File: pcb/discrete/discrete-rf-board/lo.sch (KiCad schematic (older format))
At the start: 52 parts, among them J14 UFL, J15 UFL, Q11 BFU520R, U5 ADF4360-7BCPZRL7, U6 HHM17147A1, X1 ECS-5032MV-100-BN-TR

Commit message: Autofill
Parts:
- C100, C101, C106, C107, C211, C94: footprint (none) -> Capacitor_SMD:C_0402_1005Metric; Mouser (none) -> 791-RF15N101J250CT
- R72, R74: footprint (none) -> Capacitor_SMD:C_0402_1005Metric; Mouser (none) -> 71-CRCW04020000Z0EDC
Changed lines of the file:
@@
 F 0 "R72" H 7680 4220 50  0000 L CNN
 F 1 "0R" H 7680 4160 50  0000 L CNN
-F 2 "" H 7650 4200 50  0001 C CNN
+F 2 "Capacitor_SMD:C_0402_1005Metric" H 7650 4200 50  0001 C CNN
 F 3 "~" H 7650 4200 50  0001 C CNN
+F 4 "71-CRCW04020000Z0EDC" H 7650 4200 50  0001 C CNN "Mouser"
 	1    7650 4200
 	0    -1   1    0
@@
 F 0 "R74" H 8180 4220 50  0000 L CNN
 F 1 "0R" H 8180 4160 50  0000 L CNN
-F 2 "" H 8150 4200 50  0001 C CNN
+F 2 "Capacitor_SMD:C_0402_1005Metric" H 8150 4200 50  0001 C CNN
 F 3 "~" H 8150 4200 50  0001 C CNN
+F 4 "71-CRCW04020000Z0EDC" H 8150 4200 50  0001 C CNN "Mouser"
 	1    8150 4200
 	0    -1   1    0
@@
 F 0 "C106" H 9610 3970 50  0000 L CNN
 F 1 "100 pF" H 9610 3820 50  0000 L CNN
-F 2 "" H 9600 3900 50  0001 C CNN
+F 2 "Capacitor_SMD:C_0402_1005Metric" H 9600 3900 50  0001 C CNN
 F 3 "~" H 9600 3900 50  0001 C CNN
+F 4 "791-RF15N101J250CT " H 9600 3900 50  0001 C CNN "Mouser"
 	1    9600 3900
 	0    -1   -1   0
@@
 F 0 "C107" H 10160 3070 50  0000 L CNN
 F 1 "100 pF" H 10160 2920 50  0000 L CNN
-F 2 "" H 10150 3000 50  0001 C CNN
+F 2 "Capacitor_SMD:C_0402_1005Metric" H 10150 3000 50  0001 C CNN
 F 3 "~" H 10150 3000 50  0001 C CNN
+F 4 "791-RF15N101J250CT " H 10150 3000 50  0001 C CNN "Mouser"
 	1    10150 3000
 	1    0    0    -1
@@
 F 0 "C94" H 5410 2320 50  0000 L CNN
 F 1 "100 pF" H 5410 2170 50  0000 L CNN
-F 2 "" H 5400 2250 50  0001 C CNN
+F 2 "Capacitor_SMD:C_0402_1005Metric" H 5400 2250 50  0001 C CNN
 F 3 "~" H 5400 2250 50  0001 C CNN
+F 4 "791-RF15N101J250CT " H 5400 2250 50  0001 C CNN "Mouser"
 	1    5400 2250
 	1    0    0    -1
@@
 F 0 "C100" H 6160 2320 50  0000 L CNN
 F 1 "100 pF" H 6160 2170 50  0000 L CNN
-F 2 "" H 6150 2250 50  0001 C CNN
+F 2 "Capacitor_SMD:C_0402_1005Metric" H 6150 2250 50  0001 C CNN
 F 3 "~" H 6150 2250 50  0001 C CNN
+F 4 "791-RF15N101J250CT " H 6150 2250 50  0001 C CNN "Mouser"
 	1    6150 2250
 	1    0    0    -1
@@
 F 0 "C101" H 6560 2320 50  0000 L CNN
 F 1 "100 pF" H 6560 2170 50  0000 L CNN
-F 2 "" H 6550 2250 50  0001 C CNN
+F 2 "Capacitor_SMD:C_0402_1005Metric" H 6550 2250 50  0001 C CNN
 F 3 "~" H 6550 2250 50  0001 C CNN
+F 4 "791-RF15N101J250CT " H 6550 2250 50  0001 C CNN "Mouser"
 	1    6550 2250
 	1    0    0    -1
@@
 F 0 "C211" H 9560 4770 50  0000 L CNN
 F 1 "100 pF" H 9560 4620 50  0000 L CNN
-F 2 "" H 9550 4700 50  0001 C CNN
+F 2 "Capacitor_SMD:C_0402_1005Metric" H 9550 4700 50  0001 C CNN
 F 3 "~" H 9550 4700 50  0001 C CNN
+F 4 "791-RF15N101J250CT " H 9550 4700 50  0001 C CNN "Mouser"
 	1    9550 4700
 	1    0    0    -1

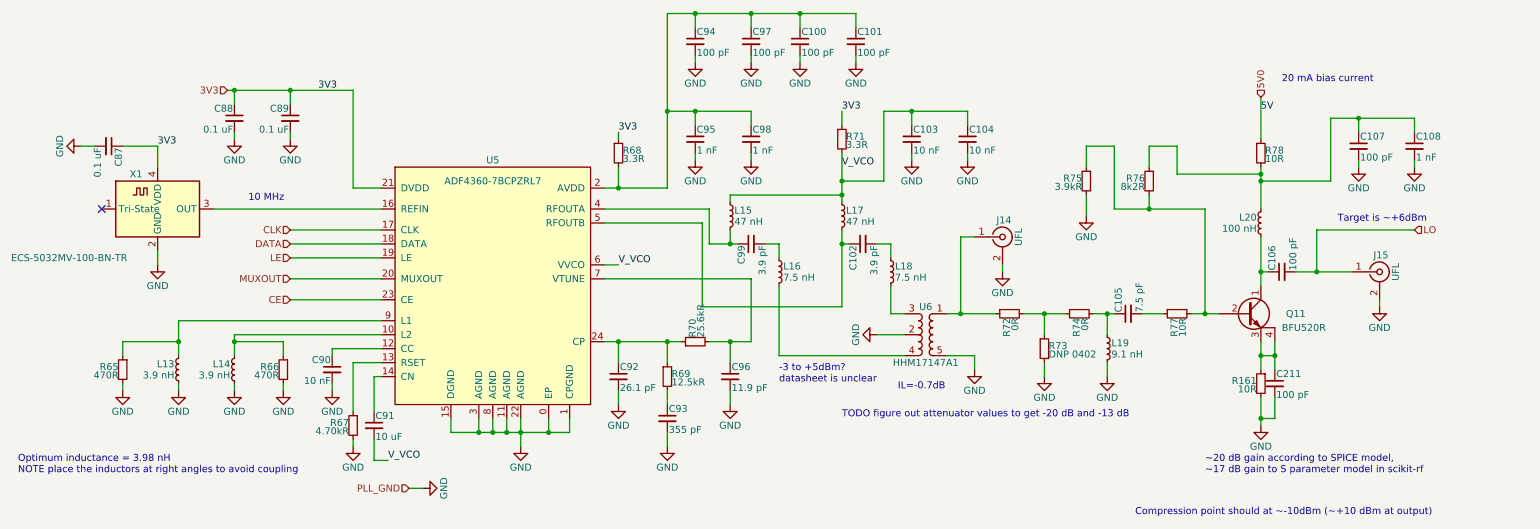
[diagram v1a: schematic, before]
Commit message: Add more footprints, saving before autofill
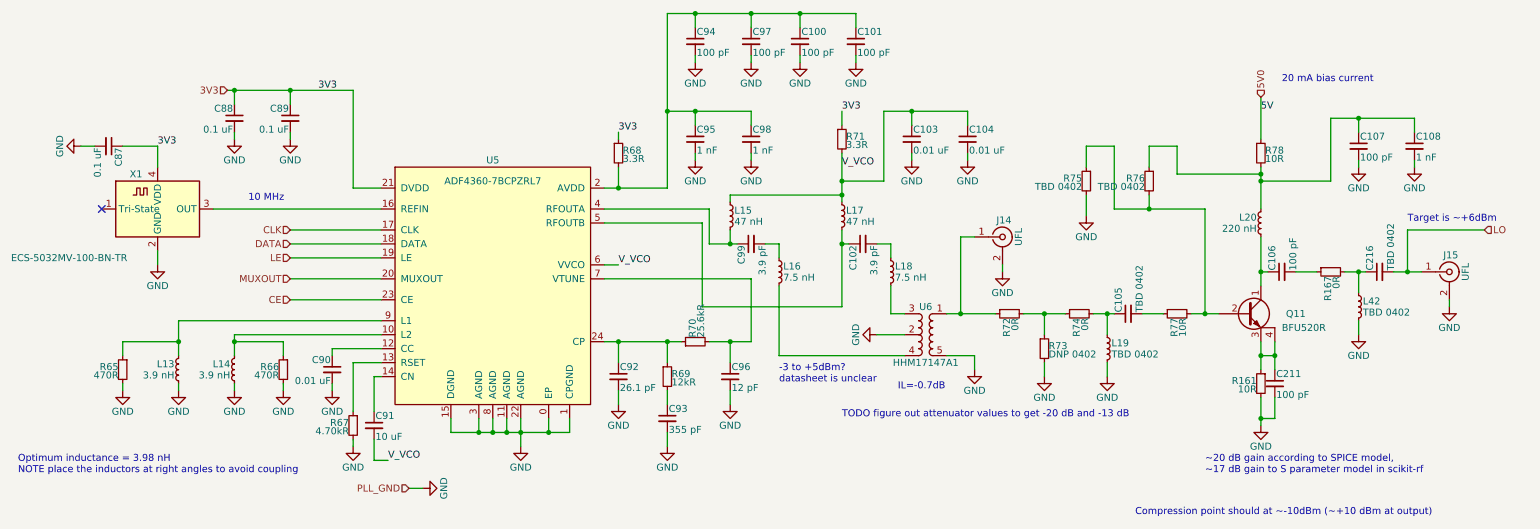
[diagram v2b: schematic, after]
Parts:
- added C216: TBD 0402, symbol Device:C_Small
- added L42: TBD 0402, symbol Device:L_Small
- added R167: 0R, Capacitor_SMD:C_0402_1005Metric, symbol Device:R_Small
- C103, C104, C90: value 10 nF -> 0.01 uF
- C105: value 7.5 pF -> TBD 0402
- C91: footprint (none) -> Capacitor_SMD:C_0805_2012Metric_Pad1.15x1.40mm_HandSolder; Mouser (none) -> 81-GRM21BC81C106KE5L
- C96: value 11.9 pF -> 12 pF; footprint (none) -> Capacitor_SMD:C_0402_1005Metric; Mouser (none) -> 791-0402N120F500CT
- L19: value 9.1 nH -> TBD 0402
- L20: value 100 nH -> 220 nH
- R69: value 12.5kR -> 12kR; footprint (none) -> Resistor_SMD:R_0603_1608Metric_Pad1.05x0.95mm_HandSolder; Mouser (none) -> 603-RC0603FR-0712KL
- R75: value 3.9kR -> TBD 0402
- R76: value 8k2R -> TBD 0402
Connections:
- net GND: now also L42.2
- net LO: now also C216.2; no longer C106.2
- new net: C106.2, R167.1
- new net: C216.1, L42.1, R167.2
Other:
- moved on the sheet: J15
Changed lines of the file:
@@
 P 2800 4600
 F 0 "C90" H 2810 4670 50  0000 L CNN
-F 1 "10 nF" H 2810 4520 50  0000 L CNN
+F 1 "0.01 uF" H 2810 4520 50  0000 L CNN
 F 2 "" H 2800 4600 50  0001 C CNN
 F 3 "~" H 2800 4600 50  0001 C CNN
@@
 F 0 "C91" H 3110 5070 50  0000 L CNN
 F 1 "10 uF" H 3110 4920 50  0000 L CNN
-F 2 "" H 3100 5000 50  0001 C CNN
+F 2 "Capacitor_SMD:C_0805_2012Metric_Pad1.15x1.40mm_HandSolder" H 3100 5000 50  0001 C CNN
 F 3 "~" H 3100 5000 50  0001 C CNN
+F 4 "81-GRM21BC81C106KE5L" H 3100 5000 50  0001 C CNN "Mouser"
 	1    3100 5000
 	1    0    0    -1
@@
 P 6950 2950
 F 0 "C103" H 6960 3020 50  0000 L CNN
-F 1 "10 nF" H 6960 2870 50  0000 L CNN
+F 1 "0.01 uF" H 6960 2870 50  0000 L CNN
 F 2 "" H 6950 2950 50  0001 C CNN
 F 3 "~" H 6950 2950 50  0001 C CNN
@@
 P 7350 2950
 F 0 "C104" H 7360 3020 50  0000 L CNN
-F 1 "10 nF" H 7360 2870 50  0000 L CNN
+F 1 "0.01 uF" H 7360 2870 50  0000 L CNN
 F 2 "" H 7350 2950 50  0001 C CNN
 F 3 "~" H 7350 2950 50  0001 C CNN
@@
 Text Notes 6850 4750 0    50   ~ 0
 IL=-0.7dB
-Text HLabel 10550 3600 2    50   Input ~ 0
+Text HLabel 11050 3600 2    50   Input ~ 0
 LO
 $Comp
@@
 L Connector:Conn_Coaxial J15
 U 1 1 5CB1681E
-P 10300 3900
-F 0 "J15" H 10310 4020 50  0000 C CNN
-F 1 "UFL" V 10415 3900 50  0000 C CNN
-F 2 "discrete_footprints:2337019-1" H 10300 3900 50  0001 C CNN
-F 3 " ~" H 10300 3900 50  0001 C CNN
-F 4 " 571-2337019-1" H 10300 3900 50  0001 C CNN "Mouser"
-	1    10300 3900
+P 10800 3900
+F 0 "J15" H 10810 4020 50  0000 C CNN
+F 1 "UFL" V 10915 3900 50  0000 C CNN
+F 2 "discrete_footprints:2337019-1" H 10800 3900 50  0001 C CNN
+F 3 " ~" H 10800 3900 50  0001 C CNN
+F 4 " 571-2337019-1" H 10800 3900 50  0001 C CNN "Mouser"
+	1    10800 3900
 	1    0    0    -1
 $EndComp
@@
 L power:GND #PWR0129
 U 1 1 5CB16963
-P 10300 4150
-F 0 "#PWR0129" H 10300 3900 50  0001 C CNN
-F 1 "GND" H 10300 4000 50  0000 C CNN
-F 2 "" H 10300 4150 50  0001 C CNN
-F 3 "" H 10300 4150 50  0001 C CNN
-	1    10300 4150
-	1    0    0    -1
-$EndComp
-Wire Wire Line
-	10300 4100 10300 4150
+P 10800 4150
+F 0 "#PWR0129" H 10800 3900 50  0001 C CNN
+F 1 "GND" H 10800 4000 50  0000 C CNN
+F 2 "" H 10800 4150 50  0001 C CNN
+F 3 "" H 10800 4150 50  0001 C CNN
+	1    10800 4150
+	1    0    0    -1
+$EndComp
+Wire Wire Line
+	10800 4100 10800 4150
 Text Notes 6000 4700 0    50   ~ 0
 -3 to +5dBm?\ndatasheet is unclear
 Wire Wire Line
-	10550 3600 9850 3600
-Wire Wire Line
-	9850 3600 9850 3900
+	11050 3600 10500 3600
 $Comp
 L Device:R_Small R72
@@
 P 8350 4450
 F 0 "L19" H 8380 4490 50  0000 L CNN
-F 1 "9.1 nH" H 8380 4410 50  0000 L CNN
+F 1 "TBD 0402" H 8380 4410 50  0000 L CNN
 F 2 "" H 8350 4450 50  0001 C CNN
 F 3 "~" H 8350 4450 50  0001 C CNN
@@
 P 8500 4200
 F 0 "C105" H 8510 4270 50  0000 L CNN
-F 1 "7.5 pF" H 8510 4120 50  0000 L CNN
+F 1 "TBD 0402" H 8510 4120 50  0000 L CNN
 F 2 "" H 8500 4200 50  0001 C CNN
 F 3 "~" H 8500 4200 50  0001 C CNN
@@
 P 8200 3250
 F 0 "R75" H 8230 3270 50  0000 L CNN
-F 1 "3.9kR" H 8230 3210 50  0000 L CNN
+F 1 "TBD 0402" H 8230 3210 50  0000 L CNN
 F 2 "" H 8200 3250 50  0001 C CNN
 F 3 "~" H 8200 3250 50  0001 C CNN
@@
 Wire Wire Line
 	9700 3900 9850 3900
-Connection ~ 9850 3900
 Wire Wire Line
 	9500 3900 9450 3900
@@
 P 9450 3550
 F 0 "L20" H 9480 3590 50  0000 L CNN
-F 1 "100 nH" H 9480 3510 50  0000 L CNN
+F 1 "220 nH" H 9480 3510 50  0000 L CNN
 F 2 "" H 9450 3550 50  0001 C CNN
 F 3 "~" H 9450 3550 50  0001 C CNN
@@
 P 8650 3250
 F 0 "R76" H 8680 3270 50  0000 L CNN
-F 1 "8k2R" H 8680 3210 50  0000 L CNN
+F 1 "TBD 0402" H 8680 3210 50  0000 L CNN
 F 2 "" H 8650 3250 50  0001 C CNN
 F 3 "~" H 8650 3250 50  0001 C CNN
@@
 Wire Wire Line
 	9450 2650 9450 2950
-Wire Wire Line
-	9850 3900 10100 3900
 $Comp
 L Device:R_Small R77
@@
 Text Notes 6450 4950 0    50   ~ 0
 TODO figure out attenuator values to get -20 dB and -13 dB
-Text Notes 10000 3550 0    50   ~ 0
+Text Notes 10500 3550 0    50   ~ 0
 Target is ~~+6dBm
 $Comp
@@
 P 5200 4650
 F 0 "R69" H 5230 4670 50  0000 L CNN
-F 1 "12.5kR" H 5230 4610 50  0000 L CNN
-F 2 "" H 5200 4650 50  0001 C CNN
+F 1 "12kR" H 5230 4610 50  0000 L CNN
+F 2 "Resistor_SMD:R_0603_1608Metric_Pad1.05x0.95mm_HandSolder" H 5200 4650 50  0001 C CNN
 F 3 "~" H 5200 4650 50  0001 C CNN
+F 4 "603-RC0603FR-0712KL" H 5200 4650 50  0001 C CNN "Mouser"
 	1    5200 4650
 	1    0    0    -1
@@
 P 5650 4650
 F 0 "C96" H 5660 4720 50  0000 L CNN
-F 1 "11.9 pF" H 5660 4570 50  0000 L CNN
-F 2 "" H 5650 4650 50  0001 C CNN
+F 1 "12 pF" H 5660 4570 50  0000 L CNN
+F 2 "Capacitor_SMD:C_0402_1005Metric" H 5650 4650 50  0001 C CNN
 F 3 "~" H 5650 4650 50  0001 C CNN
+F 4 "791-0402N120F500CT" H 5650 4650 50  0001 C CNN "Mouser"
 	1    5650 4650
 	1    0    0    -1
@@
 	1    0    0    -1
 $EndComp
+$Comp
+L Device:R_Small R167
+U 1 1 5D94440F
+P 9950 3900
+F 0 "R167" H 9980 3920 50  0000 L CNN
+F 1 "0R" H 9980 3860 50  0000 L CNN
+F 2 "Capacitor_SMD:C_0402_1005Metric" H 9950 3900 50  0001 C CNN
+F 3 "~" H 9950 3900 50  0001 C CNN
+F 4 "71-CRCW04020000Z0EDC" H 9950 3900 50  0001 C CNN "Mouser"
+	1    9950 3900
+	0    -1   1    0
+$EndComp
+$Comp
+L Device:L_Small L42
+U 1 1 5D944416
+P 10150 4150
+F 0 "L42" H 10180 4190 50  0000 L CNN
+F 1 "TBD 0402" H 10180 4110 50  0000 L CNN
+F 2 "" H 10150 4150 50  0001 C CNN
+F 3 "~" H 10150 4150 50  0001 C CNN
+	1    10150 4150
+	1    0    0    -1
+$EndComp
+$Comp
+L Device:C_Small C216
+U 1 1 5D94441C
+P 10300 3900
+F 0 "C216" H 10310 3970 50  0000 L CNN
+F 1 "TBD 0402" H 10310 3820 50  0000 L CNN
+F 2 "" H 10300 3900 50  0001 C CNN
+F 3 "~" H 10300 3900 50  0001 C CNN
+	1    10300 3900
+	0    -1   -1   0
+$EndComp
+Wire Wire Line
+	10050 3900 10150 3900
+Wire Wire Line
+	10150 3900 10150 4050
+Connection ~ 10150 3900
+Wire Wire Line
+	10150 3900 10200 3900
+$Comp
+L power:GND #PWR0260
+U 1 1 5D944426
+P 10150 4350
+F 0 "#PWR0260" H 10150 4100 50  0001 C CNN
+F 1 "GND" H 10150 4200 50  0000 C CNN
+F 2 "" H 10150 4350 50  0001 C CNN
+F 3 "" H 10150 4350 50  0001 C CNN
+	1    10150 4350
+	1    0    0    -1
+$EndComp
+Wire Wire Line
+	10150 4250 10150 4350
+Wire Wire Line
+	10400 3900 10500 3900
+Wire Wire Line
+	10500 3900 10500 3600
+Connection ~ 10500 3900
+Wire Wire Line
+	10500 3900 10600 3900
 $EndSCHEMATC

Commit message: Autofill
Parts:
- C103, C104, C90: footprint (none) -> Capacitor_SMD:C_0402_1005Metric; Mouser (none) -> 80-C0402C103K4R7411
- C105, C216: footprint (none) -> Capacitor_SMD:C_0402_1005Metric; Mouser (none) -> 791-RF15N1R1B500CT
- C87, C88, C89: footprint (none) -> Capacitor_SMD:C_0402_1005Metric; Mouser (none) -> 80-C0402C104M4P
- R75, R76: footprint (none) -> Resistor_SMD:R_0402_1005Metric; Mouser (none) -> NoPart
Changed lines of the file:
@@
 F 0 "C90" H 2810 4670 50  0000 L CNN
 F 1 "0.01 uF" H 2810 4520 50  0000 L CNN
-F 2 "" H 2800 4600 50  0001 C CNN
+F 2 "Capacitor_SMD:C_0402_1005Metric" H 2800 4600 50  0001 C CNN
 F 3 "~" H 2800 4600 50  0001 C CNN
+F 4 "80-C0402C103K4R7411" H 2800 4600 50  0001 C CNN "Mouser"
 	1    2800 4600
 	-1   0    0    -1
@@
 F 0 "C103" H 6960 3020 50  0000 L CNN
 F 1 "0.01 uF" H 6960 2870 50  0000 L CNN
-F 2 "" H 6950 2950 50  0001 C CNN
+F 2 "Capacitor_SMD:C_0402_1005Metric" H 6950 2950 50  0001 C CNN
 F 3 "~" H 6950 2950 50  0001 C CNN
+F 4 "80-C0402C103K4R7411" H 6950 2950 50  0001 C CNN "Mouser"
 	1    6950 2950
 	1    0    0    -1
@@
 F 0 "C104" H 7360 3020 50  0000 L CNN
 F 1 "0.01 uF" H 7360 2870 50  0000 L CNN
-F 2 "" H 7350 2950 50  0001 C CNN
+F 2 "Capacitor_SMD:C_0402_1005Metric" H 7350 2950 50  0001 C CNN
 F 3 "~" H 7350 2950 50  0001 C CNN
+F 4 "80-C0402C103K4R7411" H 7350 2950 50  0001 C CNN "Mouser"
 	1    7350 2950
 	1    0    0    -1
@@
 F 0 "C105" H 8510 4270 50  0000 L CNN
 F 1 "TBD 0402" H 8510 4120 50  0000 L CNN
-F 2 "" H 8500 4200 50  0001 C CNN
+F 2 "Capacitor_SMD:C_0402_1005Metric" H 8500 4200 50  0001 C CNN
 F 3 "~" H 8500 4200 50  0001 C CNN
+F 4 "791-RF15N1R1B500CT" H 8500 4200 50  0001 C CNN "Mouser"
 	1    8500 4200
 	0    -1   -1   0
@@
 F 0 "R75" H 8230 3270 50  0000 L CNN
 F 1 "TBD 0402" H 8230 3210 50  0000 L CNN
-F 2 "" H 8200 3250 50  0001 C CNN
+F 2 "Resistor_SMD:R_0402_1005Metric" H 8200 3250 50  0001 C CNN
 F 3 "~" H 8200 3250 50  0001 C CNN
+F 4 "NoPart" H 8200 3250 50  0001 C CNN "Mouser"
 	1    8200 3250
 	-1   0    0    -1
@@
 F 0 "R76" H 8680 3270 50  0000 L CNN
 F 1 "TBD 0402" H 8680 3210 50  0000 L CNN
-F 2 "" H 8650 3250 50  0001 C CNN
+F 2 "Resistor_SMD:R_0402_1005Metric" H 8650 3250 50  0001 C CNN
 F 3 "~" H 8650 3250 50  0001 C CNN
+F 4 "NoPart" H 8650 3250 50  0001 C CNN "Mouser"
 	1    8650 3250
 	-1   0    0    -1
@@
 F 0 "C89" H 2510 2870 50  0000 L CNN
 F 1 "0.1 uF" H 2510 2720 50  0000 L CNN
-F 2 "" H 2500 2800 50  0001 C CNN
+F 2 "Capacitor_SMD:C_0402_1005Metric" H 2500 2800 50  0001 C CNN
 F 3 "~" H 2500 2800 50  0001 C CNN
+F 4 "80-C0402C104M4P" H 2500 2800 50  0001 C CNN "Mouser"
 	1    2500 2800
 	-1   0    0    -1
@@
 F 0 "C88" H 2110 2870 50  0000 L CNN
 F 1 "0.1 uF" H 2110 2720 50  0000 L CNN
-F 2 "" H 2100 2800 50  0001 C CNN
+F 2 "Capacitor_SMD:C_0402_1005Metric" H 2100 2800 50  0001 C CNN
 F 3 "~" H 2100 2800 50  0001 C CNN
+F 4 "80-C0402C104M4P" H 2100 2800 50  0001 C CNN "Mouser"
 	1    2100 2800
 	-1   0    0    -1
@@
 F 0 "C87" H 1210 3070 50  0000 L CNN
 F 1 "0.1 uF" H 1210 2920 50  0000 L CNN
-F 2 "" H 1200 3000 50  0001 C CNN
+F 2 "Capacitor_SMD:C_0402_1005Metric" H 1200 3000 50  0001 C CNN
 F 3 "~" H 1200 3000 50  0001 C CNN
+F 4 "80-C0402C104M4P" H 1200 3000 50  0001 C CNN "Mouser"
 	1    1200 3000
 	0    1    1    0
@@
 F 0 "C216" H 10310 3970 50  0000 L CNN
 F 1 "TBD 0402" H 10310 3820 50  0000 L CNN
-F 2 "" H 10300 3900 50  0001 C CNN
+F 2 "Capacitor_SMD:C_0402_1005Metric" H 10300 3900 50  0001 C CNN
 F 3 "~" H 10300 3900 50  0001 C CNN
+F 4 "791-RF15N1R1B500CT" H 10300 3900 50  0001 C CNN "Mouser"
 	1    10300 3900
 	0    -1   -1   0

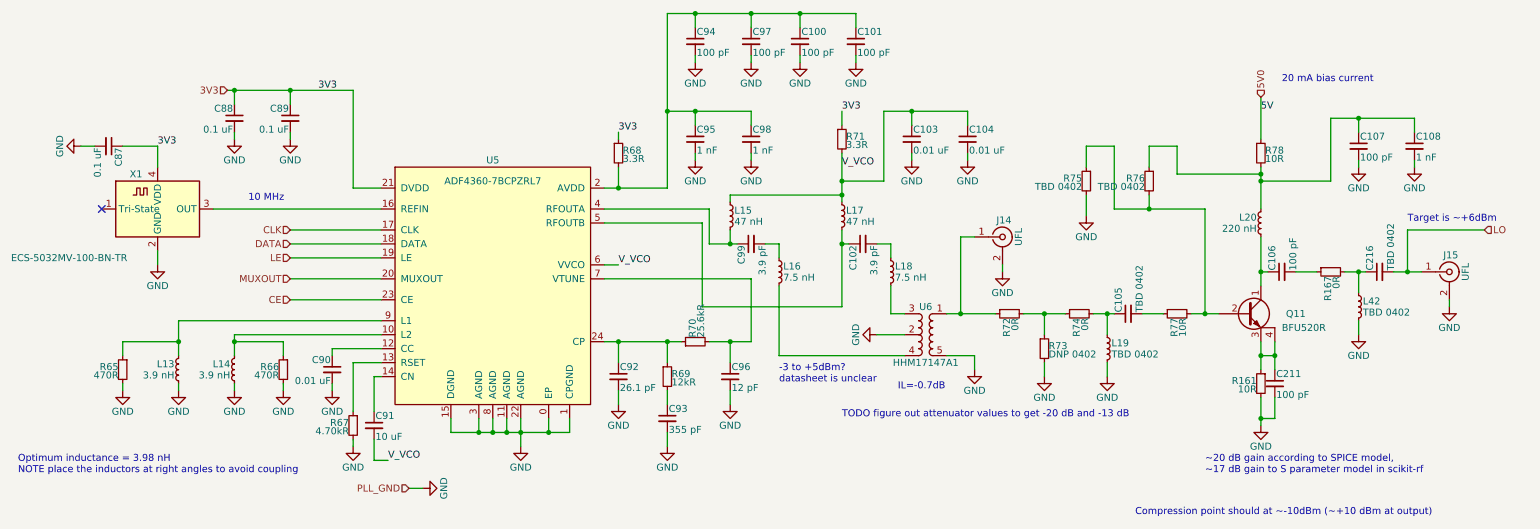
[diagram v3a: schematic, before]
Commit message: Reannotate everything; I'm trying to cut down the number of components
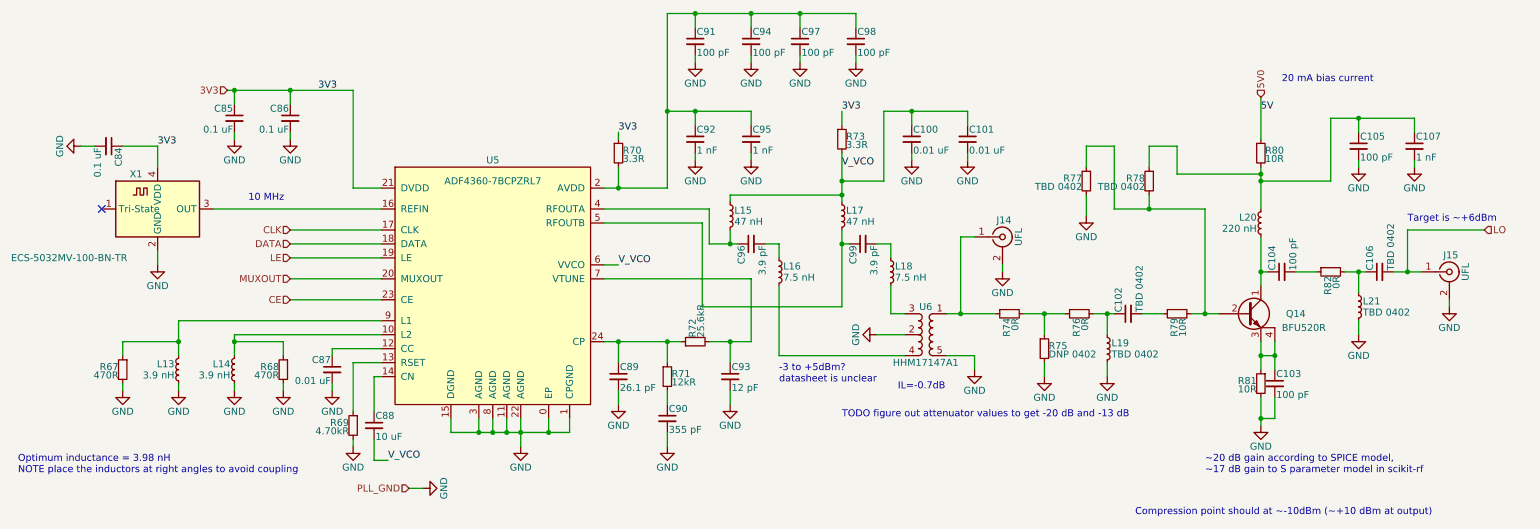
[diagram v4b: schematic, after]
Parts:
- renumbered C103 to C100, C104 to C101, C105 to C102, C211 to C103, C106 to C104, C107 to C105, C216 to C106, C108 to C107, C87 to C84, C88 to C85, C89 to C86, C90 to C87, C91 to C88, C92 to C89, C93 to C90, C94 to C91, C95 to C92, C96 to C93, C97 to C94, C98 to C95, C99 to C96, C100 to C97, C101 to C98, C102 to C99, L42 to L21, Q11 to Q14, R65 to R67, R66 to R68, R67 to R69, R68 to R70, R69 to R71, R70 to R72, R71 to R73, R72 to R74, R73 to R75, R74 to R76, R75 to R77, R76 to R78, R77 to R79, R78 to R80, R161 to R81, R167 to R82
